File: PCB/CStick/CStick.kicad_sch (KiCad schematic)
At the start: 6 parts, among them J1 Conn_01x04_Male, U1 Stickbox_Assembly

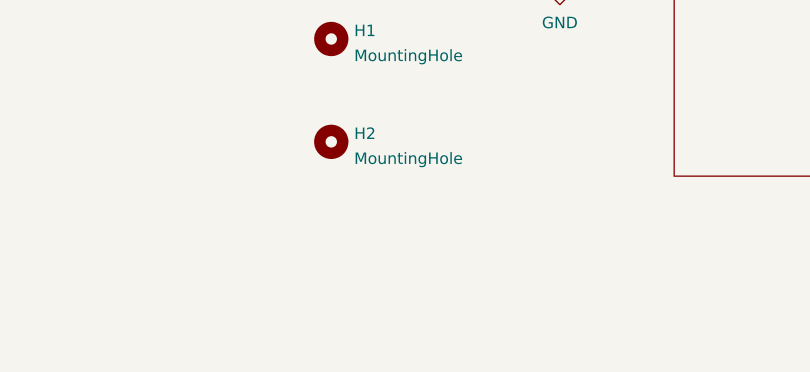
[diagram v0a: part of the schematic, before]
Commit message: Added the missing mounting holes to the c-stick
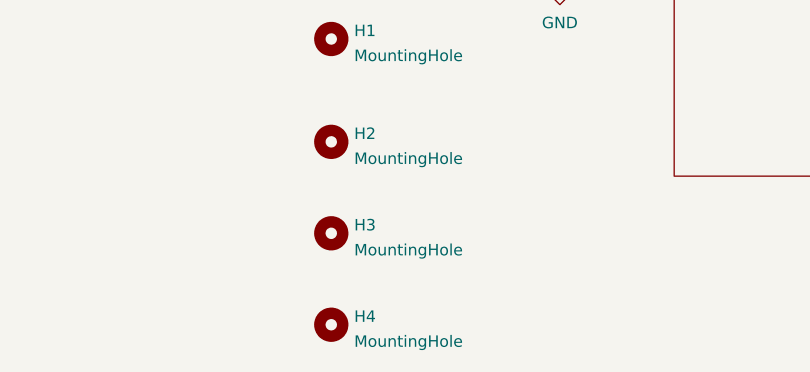
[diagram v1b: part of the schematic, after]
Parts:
- added H3, H4: MountingHole, Gamecube MB:MountingHole_2.0mm, symbol Mechanical:MountingHole
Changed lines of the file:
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@@
     (pin "2")
+  )
+  (symbol (lib_id "Mechanical:MountingHole") (at 91.44 137.16 0) (unit 1)
+    (in_bom yes) (on_board yes) (fields_autoplaced)
+    (property "Reference" "H3" (id 0) (at 93.98 136.2515 0)
+      (effects (font (size 1.27 1.27)) (justify left))
+    )
+    (property "Value" "MountingHole" (id 1) (at 93.98 139.0266 0)
+      (effects (font (size 1.27 1.27)) (justify left))
+    )
+    (property "Footprint" "Gamecube MB:MountingHole_2.0mm" (id 2) (at 91.44 137.16 0)
+      (effects (font (size 1.27 1.27)) hide)
+    )
+    (property "Datasheet" "~" (id 3) (at 91.44 137.16 0)
+      (effects (font (size 1.27 1.27)) hide)
+    )
   )
   (symbol (lib_id "Connector:Conn_01x04_Male") (at 57.15 72.39 0) (unit 1)
@@
     )
   )
+  (symbol (lib_id "Mechanical:MountingHole") (at 91.44 147.32 0) (unit 1)
+    (in_bom yes) (on_board yes) (fields_autoplaced)
+    (property "Reference" "H4" (id 0) (at 93.98 146.4115 0)
+      (effects (font (size 1.27 1.27)) (justify left))
+    )
+    (property "Value" "MountingHole" (id 1) (at 93.98 149.1866 0)
+      (effects (font (size 1.27 1.27)) (justify left))
+    )
+    (property "Footprint" "Gamecube MB:MountingHole_2.0mm" (id 2) (at 91.44 147.32 0)
+      (effects (font (size 1.27 1.27)) hide)
+    )
+    (property "Datasheet" "~" (id 3) (at 91.44 147.32 0)
+      (effects (font (size 1.27 1.27)) hide)
+    )
+  )
   (sheet_instances
     (path "/" (page "1"))
@@
       (reference "H2") (unit 1) (value "MountingHole") (footprint "Gamecube MB:MountingHole_5.2mm")
     )
+    (path "/5a8a64e8-0b04-48e4-b608-5cc887a127c8"
+      (reference "H3") (unit 1) (value "MountingHole") (footprint "Gamecube MB:MountingHole_2.0mm")
+    )
+    (path "/ff8c2871-7c9b-4de3-baec-30db09fd1a6f"
+      (reference "H4") (unit 1) (value "MountingHole") (footprint "Gamecube MB:MountingHole_2.0mm")
+    )
     (path "/61d7b681-5321-4eb3-aa94-2064a3bbd361"
